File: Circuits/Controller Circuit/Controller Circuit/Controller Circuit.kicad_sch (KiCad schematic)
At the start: 11 parts, among them J1 Joystick, SW1 SW_Push_Dual, SW2 SW_Push_Dual, SW3 SW_Push_Dual, SW4 SW_Push_Dual

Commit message: make all connections on KiCAD
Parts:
- removed DS1: OLED-128O064D, Display:OLED-128O064D, symbol Display_Graphic:OLED-128O064D
- removed R1, R2, R3: R, symbol Device:R
- removed SW1, SW2, SW3, SW4: SW_Push_Dual, Package_TO_SOT_THT:TO-220-3_Vertical, symbol Switch:SW_Push_Dual
- added R5, R6, R7: R, Resistor_THT:R_Axial_DIN0204_L3.6mm_D1.6mm_P5.08mm_Horizontal, symbol Device:R
- added SW5, SW6, SW7, SW8: SW_Push, Button_Switch_THT:SW_PUSH_6mm, symbol Switch:SW_Push
- added U1: ER_OLEDM0.91_1x-I2C, Display:ER_OLEDM0.91_1x-I2C, symbol Display_Graphic:ER_OLEDM0.91_1x-I2C
- added U2: NRF24L01_Breakout, RF_Module:nRF24L01_Breakout, symbol RF:NRF24L01_Breakout
- R4: footprint (none) -> Resistor_THT:R_Axial_DIN0204_L3.6mm_D1.6mm_P5.08mm_Horizontal
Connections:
- net D2 is gone; now on an unnamed net: R4.2
- net +5V: now also J1.2 (Pin_2), SW5.1, SW6.1, SW7.1, SW8.1
- net GND: now also A1.29 (GND), A1.4 (GND), J1.1 (Pin_1), R5.1, R6.1, R7.1, U1.1 (GND), U2.1 (GND)
- net CE/D9: now reaches A1.12 (D9)
- net CE/D9: now also U2.3 (CE)
- net CSN/D10: now reaches A1.13 (D10/CS)
- net CSN/D10: now also U2.4 (~{CSN})
- net MOSI/D11: now reaches A1.14 (D11/COPI)
- net MOSI/D11: now also U2.6 (MOSI)
- net MISO/D12: now reaches A1.15 (D12/CIPO)
- net MISO/D12: now also U2.7 (MISO)
- net SCK/D13: now reaches A1.16 (D13/SCK)
- net SCK/D13: now also U2.5 (SCK)
- net JoyVRY: now reaches A1.20 (A1)
- net JoyVRY: now also J1.4 (Pin_4)
- net JoyVRX: now reaches A1.21 (A2)
- net JoyVRX: now also J1.3 (Pin_3)
- net at A1.23 (SDA/A4): now also U1.4 (SDA)
- net at A1.24 (SCL/A5): now also U1.3 (SCL)
- net at A1.27 (VUSB/5V): now also U1.2 (VCC)
- net at A1.5 (D2): no longer names the net of A1.5 (D2)
- net at A1.5 (D2): now also SW5.2
- net Button3: now reaches A1.6 (D3)
- net Button3: now also R5.2, SW6.2
- net Button2: now reaches A1.7 (D4)
- net Button2: now also R6.2, SW7.2
- net Button1: now reaches A1.8 (D5)
- net Button1: now also R7.2, SW8.2
- net ButtonJoy: now reaches A1.9 (D6)
- net ButtonJoy: now also J1.5 (Pin_5)
- new net +3.3V: U2.2 (VCC)
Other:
- moved on the sheet: J1, R4

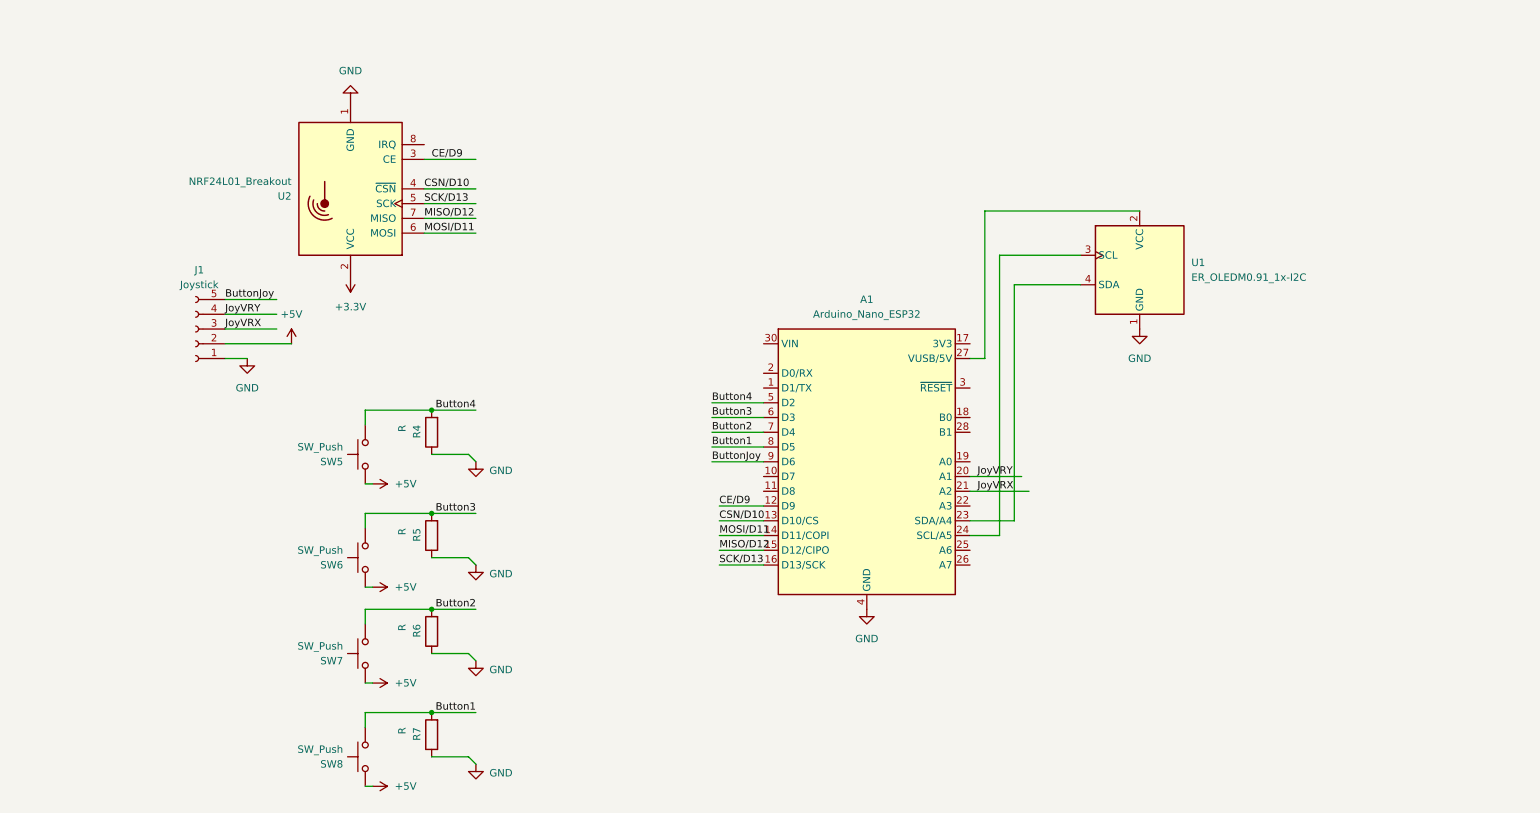
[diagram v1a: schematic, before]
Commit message: Add regulators and boosters to schematics and footprints for other parts
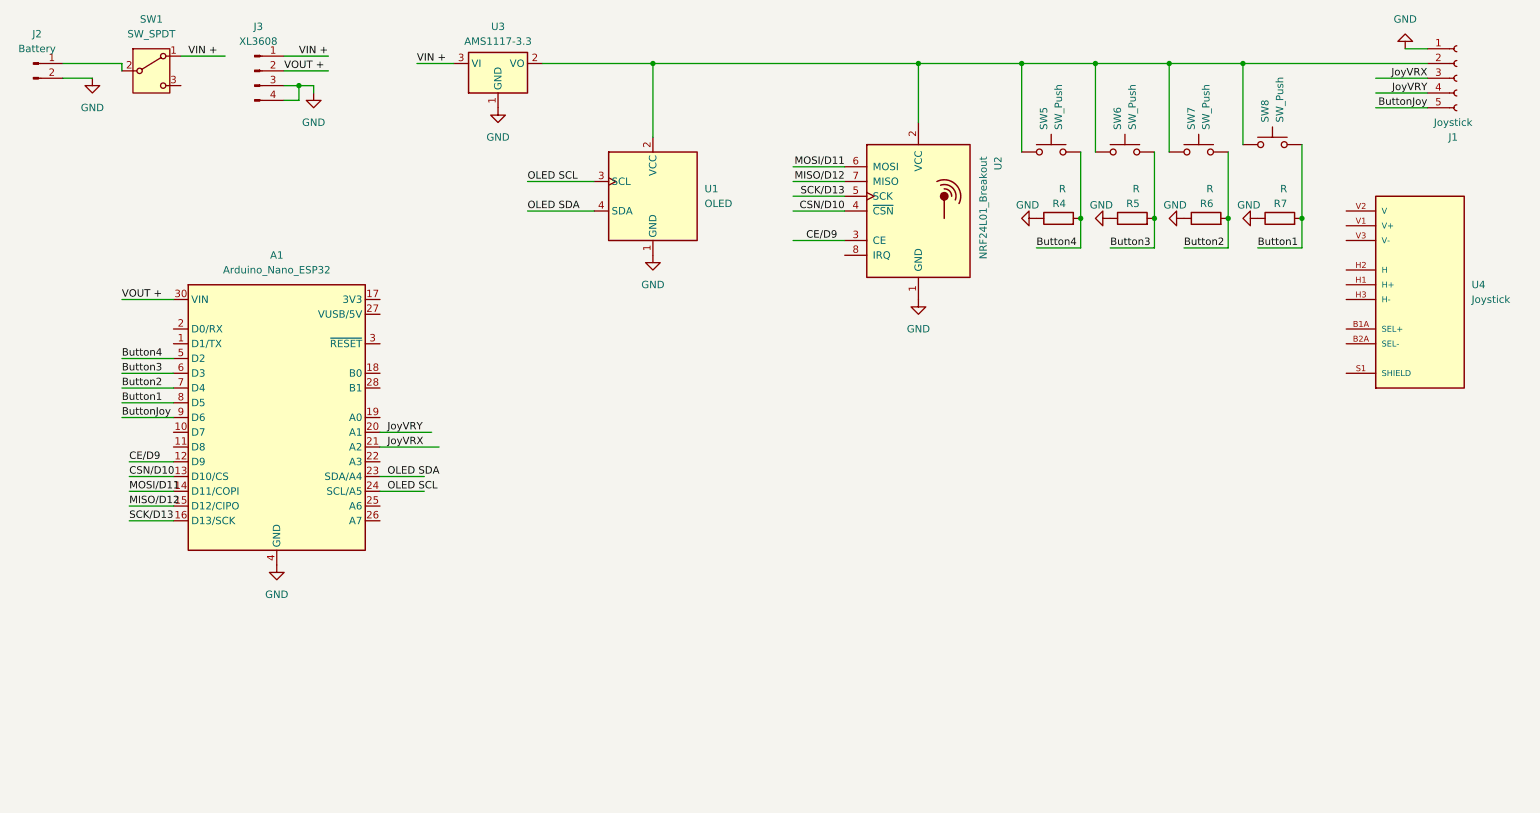
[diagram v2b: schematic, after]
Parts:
- added J2: Battery, Connector_Wire:SolderWire-6sqmm_1x02_P14mm_D3.5mm_OD7mm, symbol Connector:Conn_01x02_Pin
- added J3: XL3608, symbol Connector:Conn_01x04_Pin
- added SW1: SW_SPDT, Button_Switch_THT:SW_Slide-03_Wuerth-WS-SLTV_10x2.5x6.4_P2.54mm, symbol Switch:SW_SPDT
- added U3: AMS1117-3.3, Connector_PinSocket_2.54mm:PinSocket_1x03_P2.54mm_Horizontal, symbol Regulator_Linear:AMS1117-3.3
- added U4: Joystick, Custom Parts:XDCR_COM-09032, symbol COM-09032:COM-09032
- J1: footprint Connector:Tag-Connect_TC2030-IDC-FP_2x03_P1.27mm_Vertical -> Connector_PinSocket_2.54mm:PinSocket_1x05_P2.54mm_Horizontal
- U1: value ER_OLEDM0.91_1x-I2C -> OLED
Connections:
- net +3.3V is gone; now on an unnamed net: U2.2 (VCC)
- net +5V is gone; now on an unnamed net: J1.2 (Pin_2), SW5.1, SW6.1, SW7.1, SW8.1
- net GND: now also J2.2 (Pin_2), J3.3 (Pin_3), J3.4 (Pin_4), U3.1 (GND)
- net at U1.2 (VCC): now also U3.2 (VO); no longer A1.27 (VUSB/5V)
- net OLED SCL: now reaches A1.24 (SCL/A5), U1.3 (SCL)
- net OLED SDA: now reaches A1.23 (SDA/A4), U1.4 (SDA)
- net VOUT +: now reaches A1.30 (VIN)
- net VOUT +: now also J3.2 (Pin_2)
- new net: J2.1 (Pin_1), SW1.2 (B)
- new net: U4.S1 (SHIELD), U4.S2 (SHIELD), U4.S3 (SHIELD), U4.S4 (SHIELD)
- new net VIN +: J3.1 (Pin_1), SW1.1 (A), U3.3 (VI)
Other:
- moved on the sheet: A1, J1, R4, R5, R6, R7, SW5, SW6, SW7, SW8, U1, U2
